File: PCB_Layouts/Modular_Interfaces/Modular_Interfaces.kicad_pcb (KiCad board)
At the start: 2 copper layers, 68.2 x 53.8 mm, 37 parts, among them J1 Conn_01x03_Socket, J1 Conn_01x04_Socket, J1 RJ45_LED, J1 USB_A, J2 Conn_01x10_Socket, J3 Conn_01x10_Socket, U4 ENC28J60x-SS, Y1 25MHz

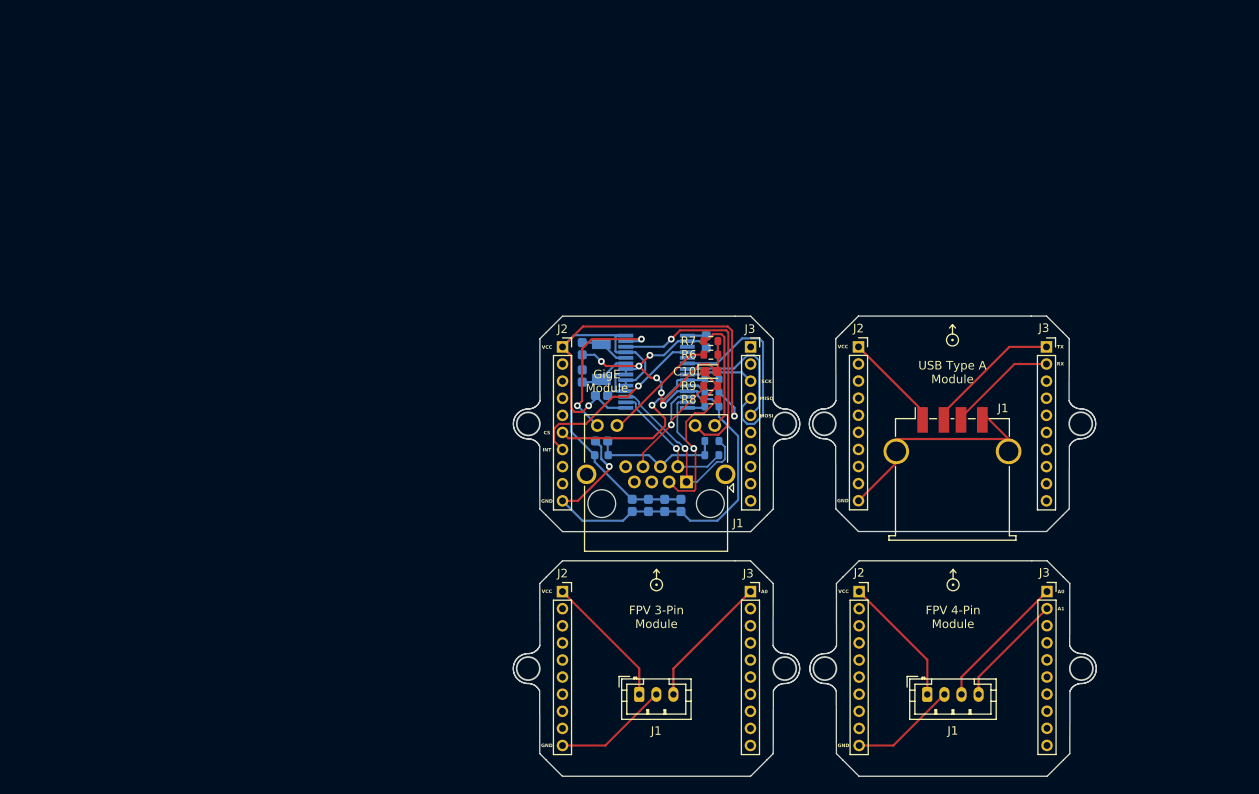
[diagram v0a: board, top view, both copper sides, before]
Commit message: Updating modular interfaces module and quote
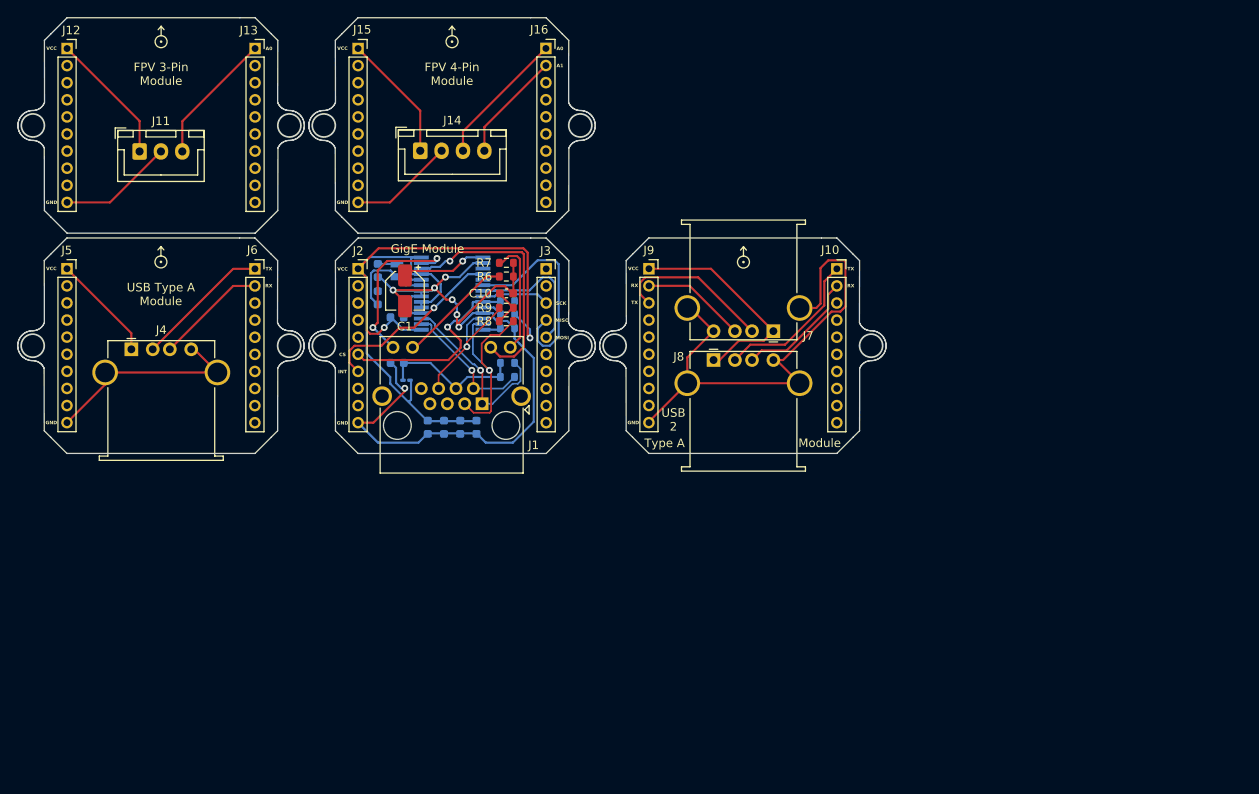
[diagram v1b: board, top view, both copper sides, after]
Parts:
- removed the EXP_ORIENTATION at (137.7, 96.2)
- removed the EXP_ORIENTATION at (172.4, 67.5)
- removed the EXP_ORIENTATION at (172.4, 96.2)
- removed the J1 at (141.2, 84.1)
- removed the J1 at (169.4, 109.0)
- removed the J1 at (135.7, 109.0)
- removed the J1 at (172.3, 83.3)
- removed the J2 at (126.7, 68.3)
- removed the J2 at (161.4, 97.0)
- removed the J2 at (161.4, 68.3)
- removed the J2 at (126.7, 97.0)
- removed the J3 at (183.4, 96.9)
- removed the J3 at (148.7, 68.3)
- removed the J3 at (148.7, 97.0)
- removed the J3 at (183.3, 68.3)
- removed U4: ENC28J60x-SS, Package_SO:SSOP-28_5.3x10.2mm_P0.65mm
- added EXP_ORIENTATION: VAL**, bitcraze:EXP_ORIENTATION, F.Cu at (113.8, 32.6)
- added EXP_ORIENTATION: VAL**, bitcraze:EXP_ORIENTATION, F.Cu at (79.8, 58.4)
- added EXP_ORIENTATION: VAL**, bitcraze:EXP_ORIENTATION, F.Cu at (147.9, 58.4)
- added EXP_ORIENTATION: VAL**, bitcraze:EXP_ORIENTATION, F.Cu at (79.8, 32.6)
- added J1: RJ45_LED, Connector_RJ:RJ45_Amphenol_RJHSE538X, F.Cu at (117.3, 75.0)
- added J10: Conn_01x10_Socket, Connector_PinSocket_2.00mm:PinSocket_1x10_P2.00mm_Vertical, F.Cu at (158.8, 59.2)
- added J11: Conn_01x03_Socket, Connector_JST:JST_XH_B3B-XH-A_1x03_P2.50mm_Vertical, F.Cu at (77.3, 45.5)
- added J12: Conn_01x10_Socket, Connector_PinSocket_2.00mm:PinSocket_1x10_P2.00mm_Vertical, F.Cu at (68.8, 33.4)
- added J13: Conn_01x10_Socket, Connector_PinSocket_2.00mm:PinSocket_1x10_P2.00mm_Vertical, F.Cu at (90.8, 33.4)
- added J14: Conn_01x04_Socket, Connector_JST:JST_XH_B4B-XH-A_1x04_P2.50mm_Vertical, F.Cu at (110.1, 45.4)
- added J15: Conn_01x10_Socket, Connector_PinSocket_2.00mm:PinSocket_1x10_P2.00mm_Vertical, F.Cu at (102.8, 33.4)
- added J16: Conn_01x10_Socket, Connector_PinSocket_2.00mm:PinSocket_1x10_P2.00mm_Vertical, F.Cu at (124.8, 33.4)
- added J2: Conn_01x10_Socket, Connector_PinSocket_2.00mm:PinSocket_1x10_P2.00mm_Vertical, F.Cu at (102.8, 59.2)
- added J3: Conn_01x10_Socket, Connector_PinSocket_2.00mm:PinSocket_1x10_P2.00mm_Vertical, F.Cu at (124.8, 59.2)
- added J4: USB_A, Connector_USB:USB_A_Stewart_SS-52100-001_Horizontal, F.Cu at (76.3, 68.6)
- added J5: Conn_01x10_Socket, Connector_PinSocket_2.00mm:PinSocket_1x10_P2.00mm_Vertical, F.Cu at (68.8, 59.2)
- added J6: Conn_01x10_Socket, Connector_PinSocket_2.00mm:PinSocket_1x10_P2.00mm_Vertical, F.Cu at (90.8, 59.2)
- added J7: USB_A, Connector_USB:USB_A_Stewart_SS-52100-001_Horizontal, F.Cu at (151.4, 66.5)
- added J8: USB_A, Connector_USB:USB_A_Stewart_SS-52100-001_Horizontal, F.Cu at (144.4, 69.9)
- added J9: Conn_01x10_Socket, Connector_PinSocket_2.00mm:PinSocket_1x10_P2.00mm_Vertical, F.Cu at (136.8, 59.2)
- added U1: ENC28J60x-SS, Package_SO:SSOP-28_5.3x10.2mm_P0.65mm, B.Cu at (113.8, 62.1)
- C1: footprint Capacitor_Tantalum_SMD:CP_EIA-1608-08_AVX-J -> Capacitor_SMD:CP_Elec_4x5.4; moved to F.Cu
- C10, C2, C3, C4, C5, C6, C7, C8: footprint Capacitor_Tantalum_SMD:CP_EIA-1608-08_AVX-J -> Capacitor_SMD:C_0603_1608Metric
- C9: value 0.01u -> 100nF; footprint Capacitor_Tantalum_SMD:CP_EIA-1608-08_AVX-J -> Capacitor_SMD:C_0603_1608Metric
- L1: footprint Inductor_SMD:L_0603_1608Metric -> Inductor_SMD:L_0201_0603Metric_Pad0.64x0.40mm_HandSolder
- Y1: footprint Crystal:Crystal_SMD_MicroCrystal_CC4V-T1A-2Pin_5.0x1.9mm -> Crystal:Crystal_SMD_MicroCrystal_CC8V-T1A-2Pin_2.0x1.2mm
- moved C1 35.7 mm to (108.3, 61.8)
- moved Y1 26.2 mm to (107.4, 59.4)
- moved R6 25.6 mm to (120.2, 60.1)
- moved R7 25.6 mm to (120.2, 58.5)
- moved R8 25.6 mm to (120.2, 65.3)
- moved C10 25.6 mm to (120.2, 62.1)
- moved C4 25.6 mm to (107.4, 64.9)
- moved C5 25.6 mm to (111.0, 77.7)
- moved C6 25.6 mm to (112.9, 77.7)
- moved R1 25.6 mm to (120.3, 63.0)
- moved R2 25.6 mm to (120.3, 64.5)
- moved R3 25.6 mm to (120.3, 66.1)
- moved R5 25.6 mm to (120.3, 71.8)
- moved C2 25.6 mm to (105.1, 62.6)
- moved C8 25.6 mm to (116.7, 77.7)
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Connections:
- C1 pad 1: (no net) -> Net-(U1-VCAP)
- C1 pad 2: (no net) -> /GND
- C10 pad 1: (no net) -> Net-(C10-Pad1)
- C10 pad 2: (no net) -> /GND
- C2 pad 1: (no net) -> /GND
- C2 pad 2: (no net) -> Net-(U1-OSC1)
- C3 pad 1: (no net) -> /GND
- C3 pad 2: (no net) -> Net-(U1-OSC2)
- C4 pad 1: (no net) -> /VCC
- C4 pad 2: (no net) -> /GND
- C5 pad 1: (no net) -> /VCC
- C5 pad 2: (no net) -> /GND
- C6 pad 1: (no net) -> /VCC
- C6 pad 2: (no net) -> /GND
- C7 pad 1: (no net) -> /VCC
- C7 pad 2: (no net) -> /GND
- C8 pad 1: (no net) -> /VCC
- C8 pad 2: (no net) -> /GND
- C9 pad 1: (no net) -> Net-(C9-Pad1)
- C9 pad 2: (no net) -> /GND
- L1 pad 1: (no net) -> /VCC
- L1 pad 2: (no net) -> Net-(C9-Pad1)
- R1 pad 1: (no net) -> /VCC
- R1 pad 2: (no net) -> /CS
- R2 pad 1: (no net) -> /VCC
- R2 pad 2: (no net) -> Net-(U1-~{RESET})
- R3 pad 1: (no net) -> Net-(U1-RBIAS)
- R3 pad 2: (no net) -> /GND
- R4 pad 1: (no net) -> Net-(C9-Pad1)
- R4 pad 2: (no net) -> /TPOUT+
- R5 pad 1: (no net) -> /TPOUT-
- R5 pad 2: (no net) -> Net-(C9-Pad1)
- R6 pad 1: (no net) -> Net-(J1-Pad11)
- R6 pad 2: (no net) -> /GND
- R7 pad 1: (no net) -> Net-(J1-Pad9)
- R7 pad 2: (no net) -> /GND
- R8 pad 1: (no net) -> Net-(C10-Pad1)
- R8 pad 2: (no net) -> /TPIN+
- R9 pad 1: (no net) -> /TPIN-
- R9 pad 2: (no net) -> Net-(C10-Pad1)
- Y1 pad 1: (no net) -> Net-(U1-OSC1)
- Y1 pad 2: (no net) -> Net-(U1-OSC2)
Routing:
- net (no net): track 655.9 -> 0.00 mm, vias 18 -> 19
- net /GND: track 0.00 -> 104.1 mm
- net /VCC: track 0.00 -> 100.9 mm
- net Net-(J7-GND): track 0.00 -> 61.9 mm
- net /LEDB: track 0.00 -> 28.5 mm
- net Net-(J7-VBUS): track 0.00 -> 26.0 mm
- net Net-(J4-GND): track 0.00 -> 25.1 mm
- net /MISO: track 0.00 -> 24.7 mm
- net /TPIN+: track 0.00 -> 24.0 mm
- net /CS: track 0.00 -> 23.7 mm
- net /INT: track 0.00 -> 22.1 mm
- net /TPOUT+: track 0.00 -> 21.6 mm
- net /LEDA: track 0.00 -> 19.7 mm
- net Net-(J7-D-): track 0.00 -> 18.8 mm
- net Net-(J10-Pin_1): track 0.00 -> 18.0 mm
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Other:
- board size 68.2 x 53.8 mm -> 101.6 x 51 mm
- board text added: "Module"
- board text added: "Type A"
- board text added: "USB 2"

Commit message: Adding Modular Interfaces No GigE module and quote
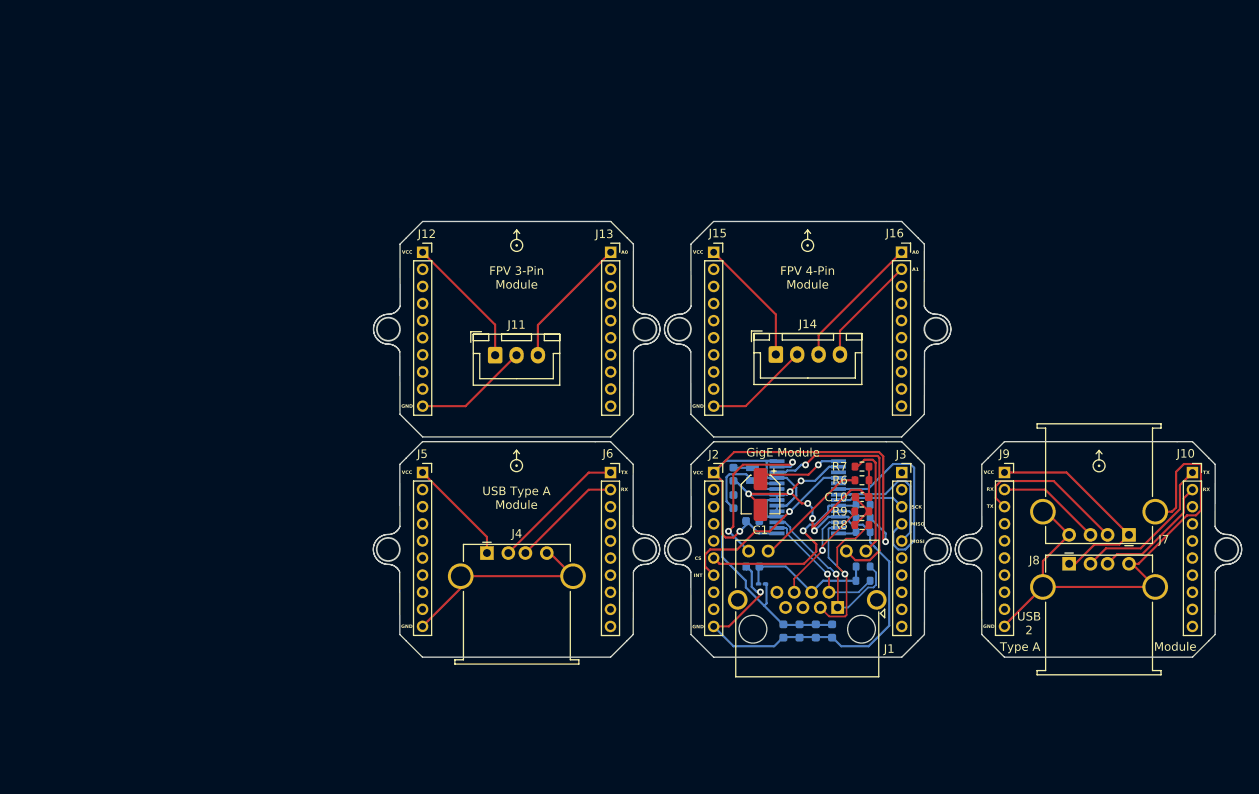
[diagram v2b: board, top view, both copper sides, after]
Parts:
- moved C8 47.9 mm to (158.3, 101.6)
- moved J15 47.9 mm to (144.4, 57.3)
- moved J16 47.9 mm to (166.4, 57.2)
- moved J3 47.9 mm to (166.4, 83.0)
- moved L1 47.9 mm to (150.1, 96.1)
- moved R4 47.9 mm to (161.9, 94.0)
- moved R6 47.9 mm to (161.8, 83.9)
- moved R7 47.9 mm to (161.8, 82.3)
- moved U1 47.9 mm to (155.4, 85.9)
- moved C10 47.9 mm to (161.8, 85.9)
- moved C3 47.9 mm to (146.7, 83.2)
- moved J2 47.9 mm to (144.4, 83.0)
- moved Y1 47.9 mm to (149.0, 83.2)
- moved C1 47.9 mm to (149.9, 85.6)
- moved C4 47.9 mm to (149.0, 88.7)
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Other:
- outline, holes or cut-outs redrawn
